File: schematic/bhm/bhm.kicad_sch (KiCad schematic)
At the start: 7 parts, among them U1 LM358, U2 ATtiny45-20P, U3 LM78L05_TO92

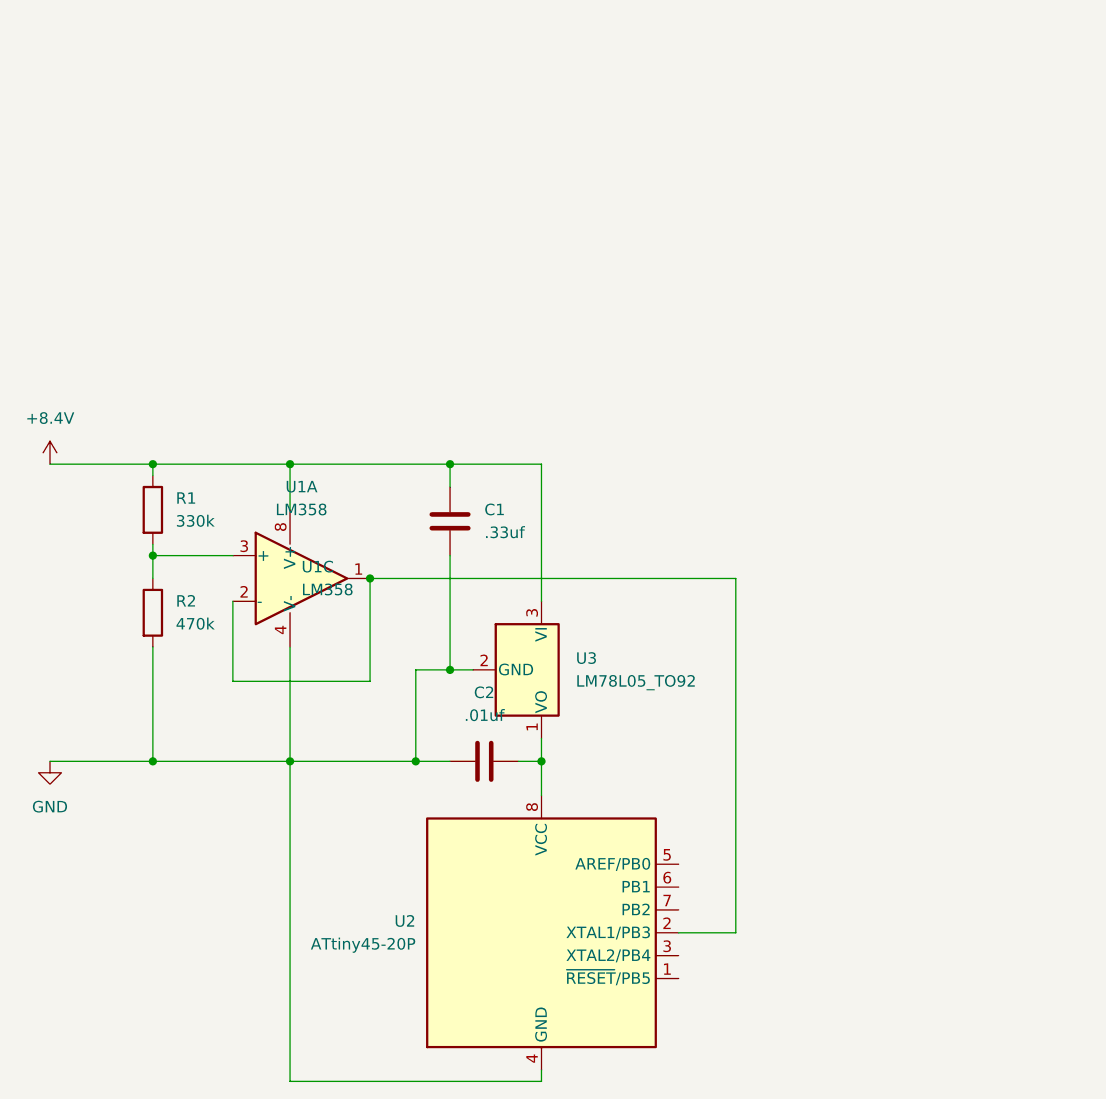
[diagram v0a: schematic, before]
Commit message: reworked to use differential opamp
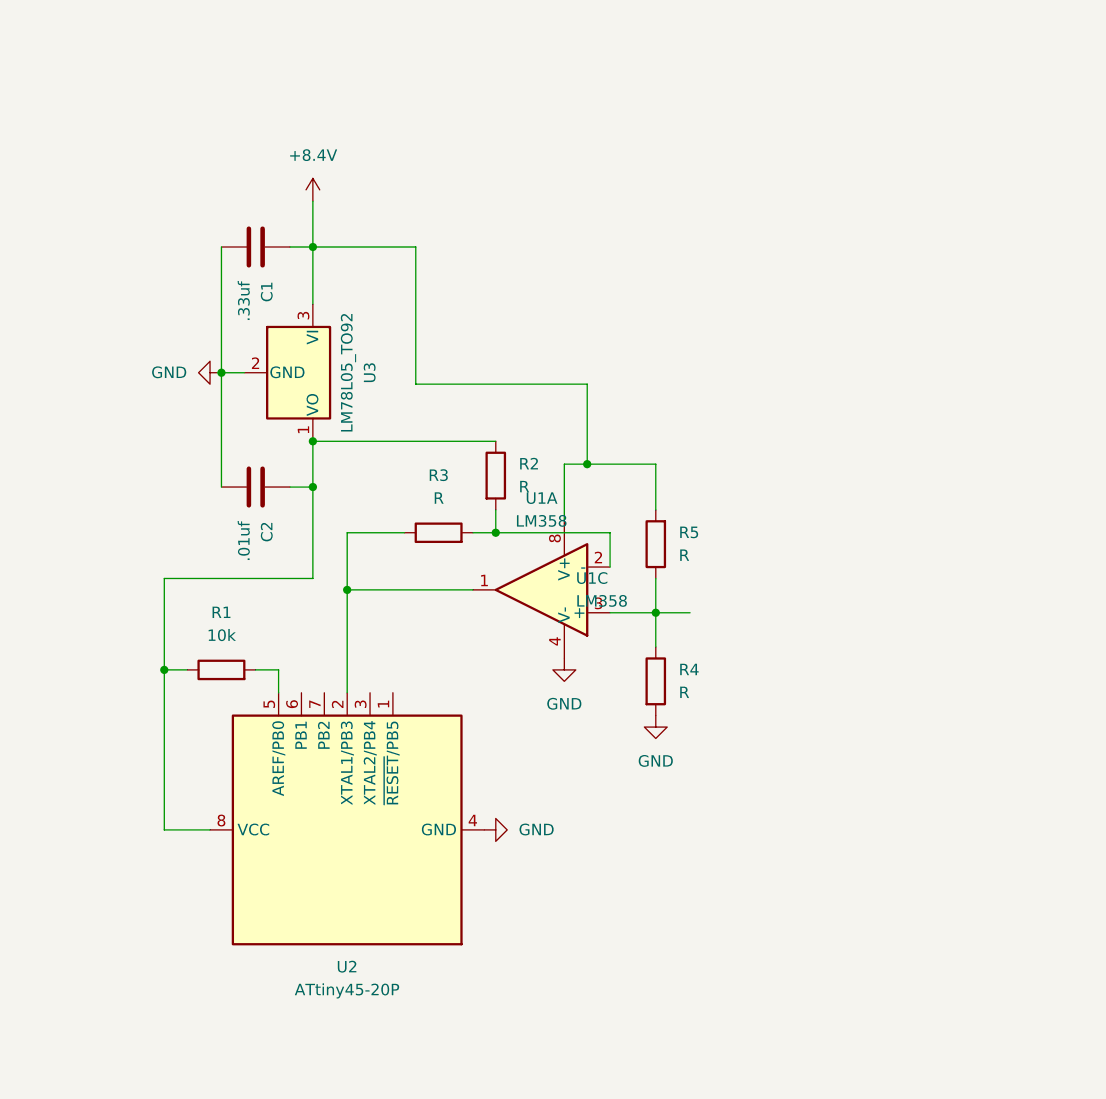
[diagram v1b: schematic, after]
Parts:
- added R3, R4, R5: R, symbol Device:R
- R1: value 330k -> 10k
- R2: value 470k -> R
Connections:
- net +8.4V: now also R5.2; no longer R1.1
- net GND: now also R4.2; no longer R2.2
- net at C2.2, U2.8 (VCC), U3.1 (VO): now also R1.1, R2.1
- net at U1.1, U2.2 (XTAL1/PB3): now also R3.1; no longer U1.2 (-)
- net at U2.5 (AREF/PB0): now also R1.2
- new net: R4.1, R5.1, U1.3 (+)
- new net: R2.2, R3.2, U1.2 (-)
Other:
- moved on the sheet: C1, C2, U1A, U1C, U2, U3

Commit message: updating schematic with footprints also fixing terrible layout
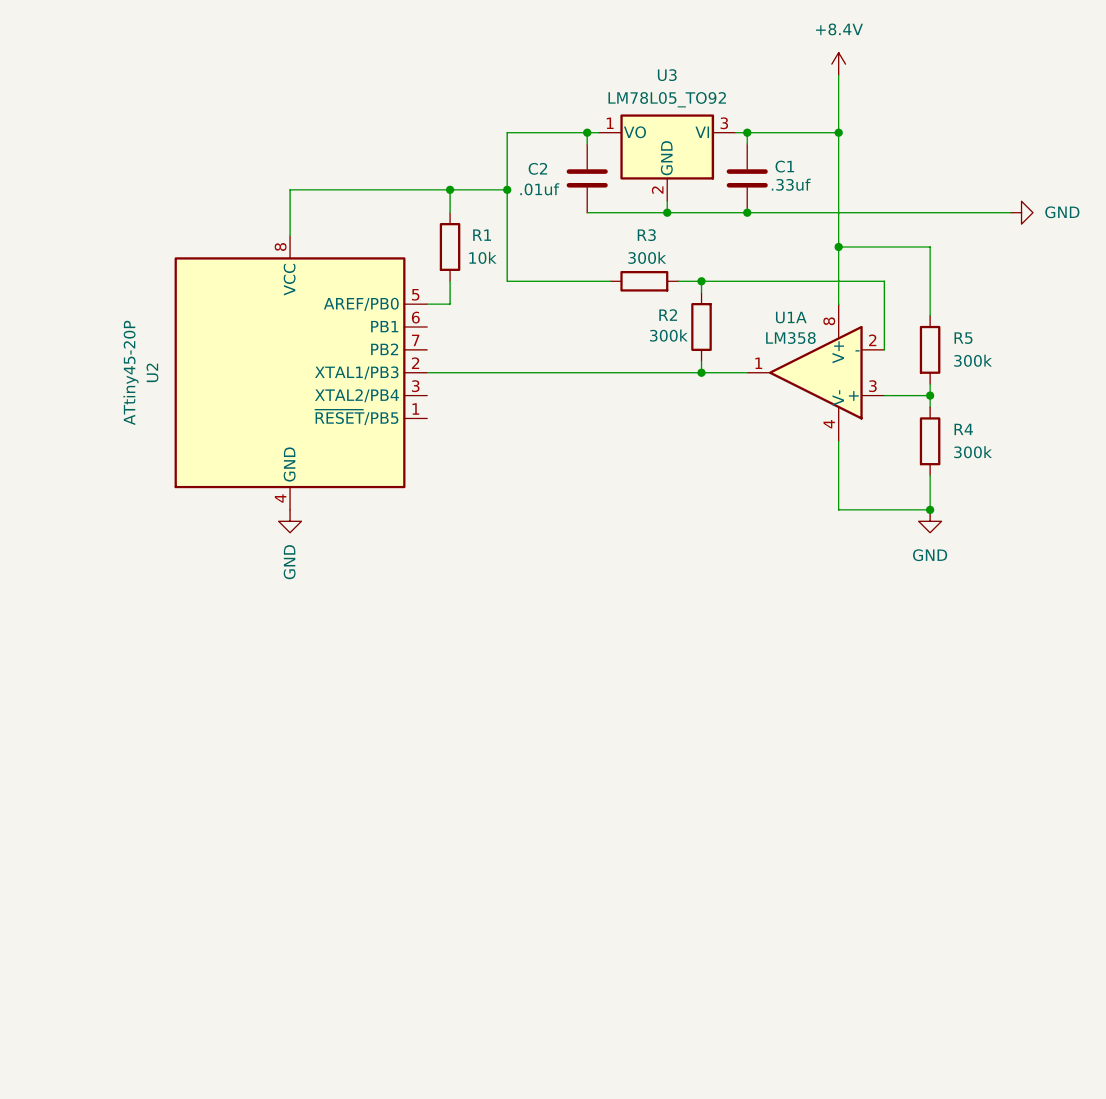
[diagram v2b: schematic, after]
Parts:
- C1: footprint (none) -> Capacitor_THT:C_Radial_D4.0mm_H7.0mm_P1.50mm
- C2: footprint (none) -> Capacitor_THT:C_Disc_D5.0mm_W2.5mm_P5.00mm
- R1: footprint (none) -> Resistor_THT:R_Axial_DIN0207_L6.3mm_D2.5mm_P7.62mm_Horizontal
- R2, R3, R4, R5: value R -> 300k; footprint (none) -> Resistor_THT:R_Axial_DIN0207_L6.3mm_D2.5mm_P7.62mm_Horizontal
- U1: footprint (none) -> Package_DIP:DIP-8_W7.62mm
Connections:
- net +8.4V: now also R5.1; no longer R5.2
- net GND: now also C2.2; no longer C2.1
- net at R4.1, U1.3 (+): now also R5.2; no longer R5.1
- net at R1.1, U2.8 (VCC), U3.1 (VO): now also C2.1, R3.1; no longer C2.2, R2.1
- net at U1.1, U2.2 (XTAL1/PB3): now also R2.1; no longer R3.1
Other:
- title: (none) -> Attiny Battery Voltage Monitor
- moved on the sheet: C1, C2, R1, R2, R3, R4, R5, U1A, U2, U3
